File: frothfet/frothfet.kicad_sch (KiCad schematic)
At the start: 9 parts

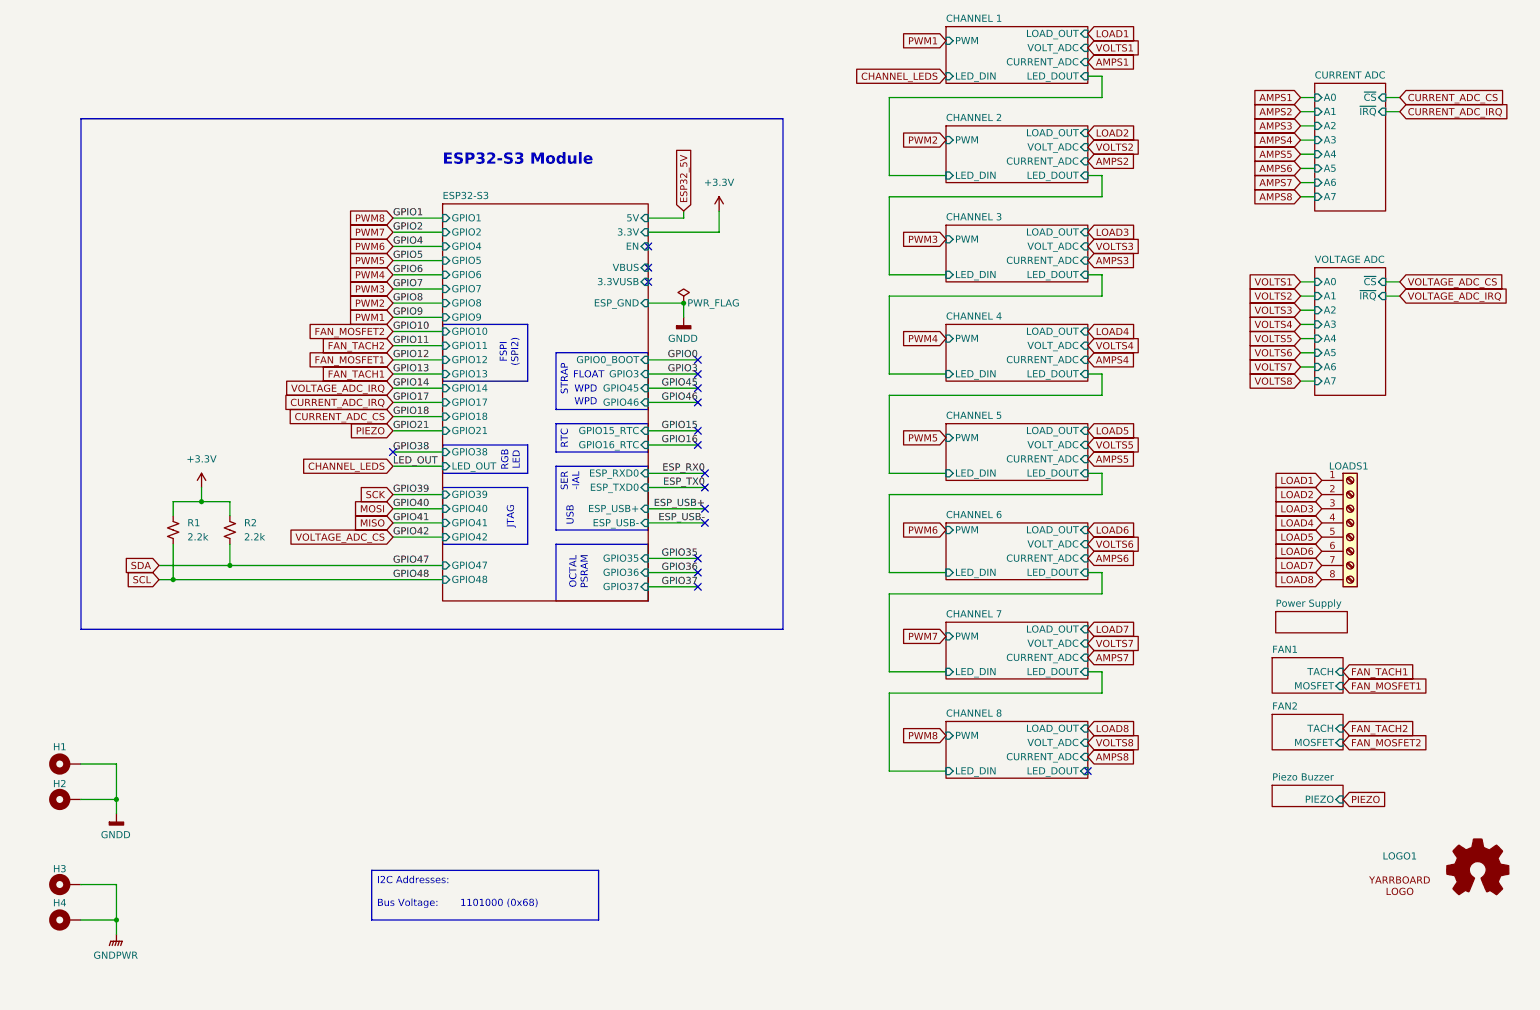
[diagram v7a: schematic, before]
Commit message: silkscreen done, erc+drc passing
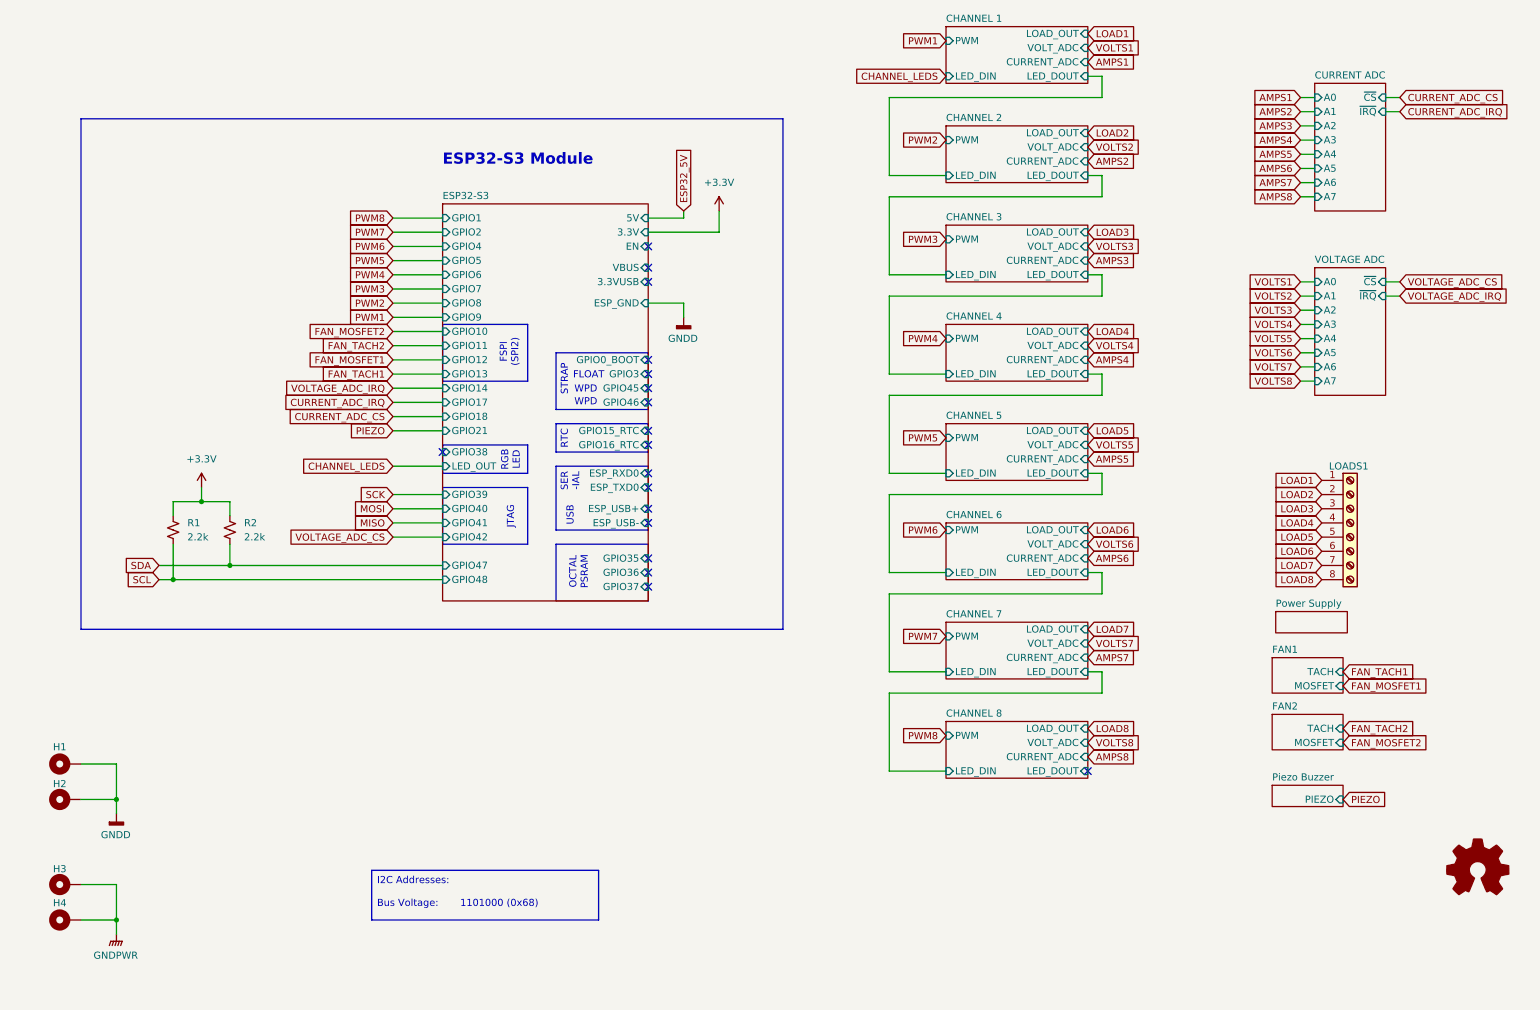
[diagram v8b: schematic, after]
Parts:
- removed LOGO1: ~, yarrboard:Logo Small, symbol yarrboard:Yarrboard
- H1, H2, H3, H4: value SMTSO30100CTJ -> ~; footprint yarrboard:Standoff-3mm -> MountingHole:MountingHole_3.2mm_M3_DIN965_Pad
- LOGO2: footprint Symbol:OSHW-Logo2_14.6x12mm_SilkScreen -> Symbol:OSHW-Logo2_7.3x6mm_SilkScreen
